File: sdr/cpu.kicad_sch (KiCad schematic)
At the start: 6 parts, among them U4 CH32V305RBT6

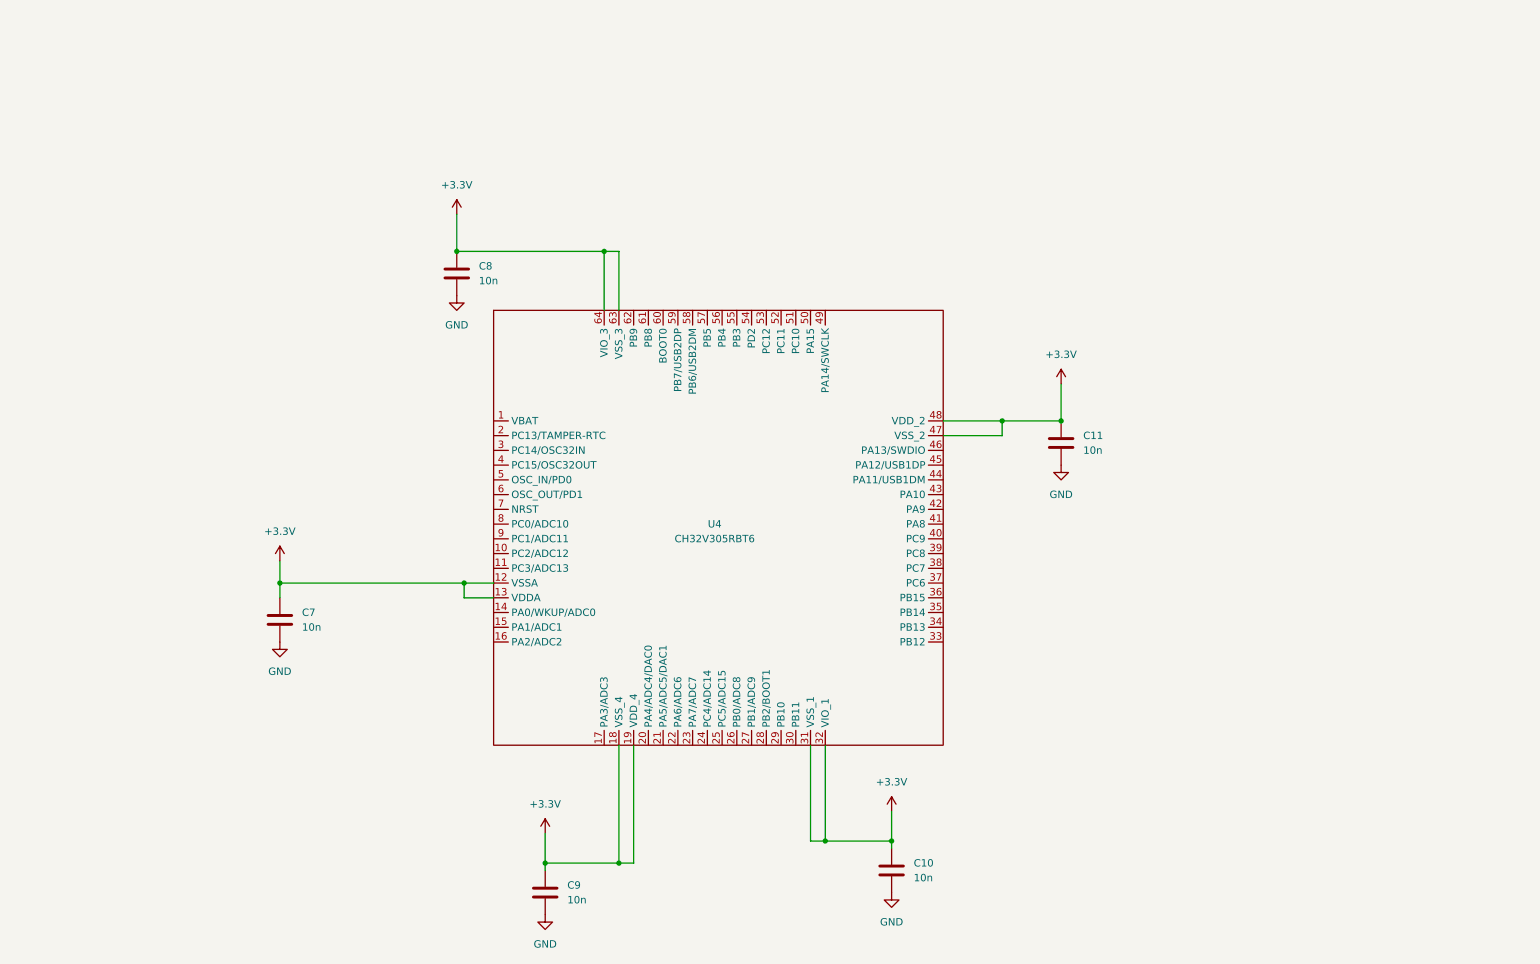
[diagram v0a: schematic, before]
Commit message: Update lots of things. Now have basic CPU as well as some crude mixers
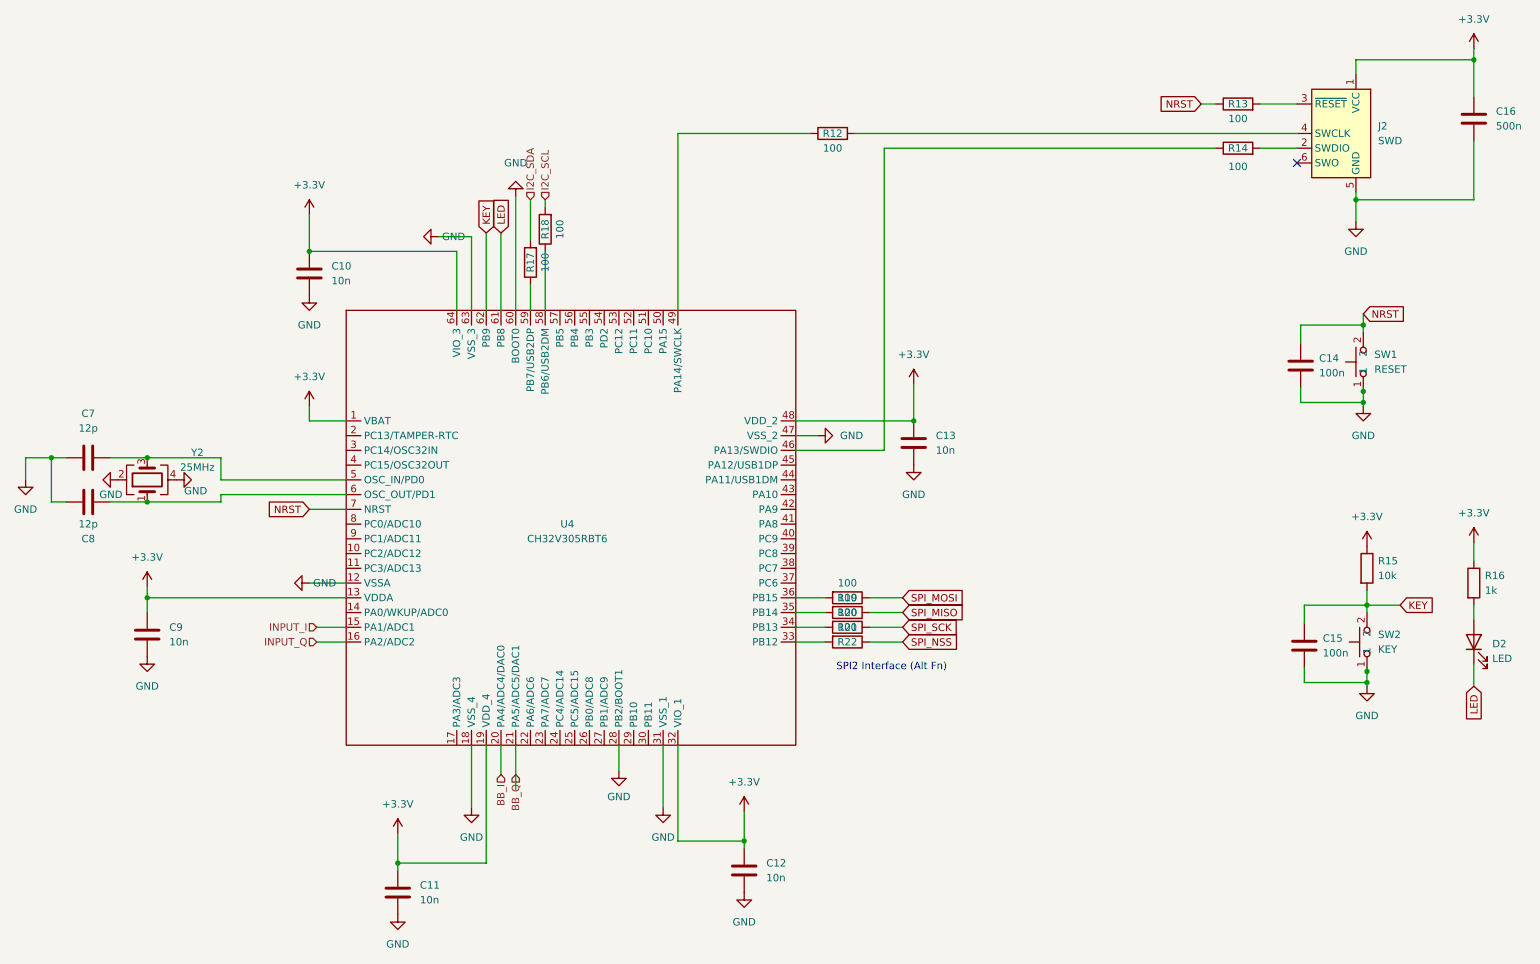
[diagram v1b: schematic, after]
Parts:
- added C14, C15: 100n, Capacitor_SMD:C_0201_0603Metric, symbol Device:C
- added C16: 500n, Capacitor_SMD:C_0201_0603Metric, symbol Device:C
- added C7, C8: 12p, Capacitor_SMD:C_0201_0603Metric, symbol Device:C
- added D2: LED, Diode_SMD:D_0603_1608Metric, symbol Device:LED
- added J2: SWD, Connector:Tag-Connect_TC2030-IDC-NL_2x03_P1.27mm_Vertical, symbol Connector:Conn_ARM_SWD_TagConnect_TC2030-NL
- added R12, R13, R14, R17, R18, R19, R20, R21, R22: 100, Resistor_SMD:R_0402_1005Metric, symbol Device:R
- added R15: 10k, Resistor_SMD:R_0402_1005Metric, symbol Device:R
- added R16: 1k, Resistor_SMD:R_0402_1005Metric, symbol Device:R
- added SW1: RESET, ZL4AA:TS-1187A-B-A-B, symbol zl4aa:TS-1187A-B-A-B
- added SW2: KEY, ZL4AA:TS-1187A-B-A-B, symbol zl4aa:TS-1187A-B-A-B
- added Y2: 25MHz, Crystal:Crystal_SMD_3225-4Pin_3.2x2.5mm, symbol Device:Crystal_GND24
- C10: renamed from C8; footprint (none) -> Capacitor_SMD:C_0201_0603Metric
- C11: renamed from C9; footprint (none) -> Capacitor_SMD:C_0201_0603Metric
- C12: renamed from C10; footprint (none) -> Capacitor_SMD:C_0201_0603Metric
- C13: renamed from C11; footprint (none) -> Capacitor_SMD:C_0201_0603Metric
- C9: renamed from C7; footprint (none) -> Capacitor_SMD:C_0201_0603Metric
- U4: footprint (none) -> Package_QFP:LQFP-64_10x10mm_P0.5mm
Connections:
- net +3.3V: now also U4.1 (VBAT), C16.1, J2.1 (VCC), R15.1, R16.1; no longer U4.12 (VSSA), U4.18 (VSS_4), U4.31 (VSS_1), U4.47 (VSS_2), U4.63 (VSS_3)
- net GND: now also U4.12 (VSSA), U4.18 (VSS_4), U4.28 (PB2/BOOT1), U4.31 (VSS_1), U4.47 (VSS_2), U4.60 (BOOT0), U4.63 (VSS_3), C14.2, C15.2, C16.2, C7.1, C8.1, J2.5 (GND), SW1.1, SW2.1, Y2.2, Y2.4
- net INPUT_I: now reaches U4.15 (PA1/ADC1)
- net INPUT_Q: now reaches U4.16 (PA2/ADC2)
- net BB_I: now reaches U4.20 (PA4/ADC4/DAC0)
- net BB_Q: now reaches U4.21 (PA5/ADC5/DAC1)
- net at U4.33 (PB12): now also R22.2
- net at U4.34 (PB13): now also R21.2
- net at U4.35 (PB14): now also R20.2
- net at U4.36 (PB15): now also R19.2
- net at U4.46 (PA13/SWDIO): now also R14.1
- net at U4.49 (PA14/SWCLK): now also R12.1
- net at U4.5 (OSC_IN/PD0): now also C7.2, Y2.3
- net at U4.58 (PB6/USB2DM): now also R18.1
- net at U4.59 (PB7/USB2DP): now also R17.1
- net at U4.6 (OSC_OUT/PD1): now also C8.2, Y2.1
- net LED: now reaches U4.61 (PB8)
- net LED: now also D2.1 (K)
- net KEY: now reaches U4.62 (PB9)
- net KEY: now also C15.1, R15.2, SW2.2
- net NRST: now reaches U4.7 (NRST)
- net NRST: now also C14.1, R13.1, SW1.2
- new net: J2.2 (SWDIO), R14.2
- new net: J2.3 (~{RESET}), R13.2
- new net: J2.4 (SWCLK), R12.2
- new net: D2.2 (A), R16.2
- new net I2C_SCL: R18.2
- new net I2C_SDA: R17.2
- new net SPI_MISO: R20.1
- new net SPI_MOSI: R19.1
- new net SPI_NSS: R22.1
- new net SPI_SCK: R21.1
- no-connect marks 0 -> 1
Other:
- note added: "SPI2 Interface (Alt Fn)"
- moved on the sheet: C10, C11, C12, C13, C9, U4

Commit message: Added ST-link 6-pin 0.1 programming header
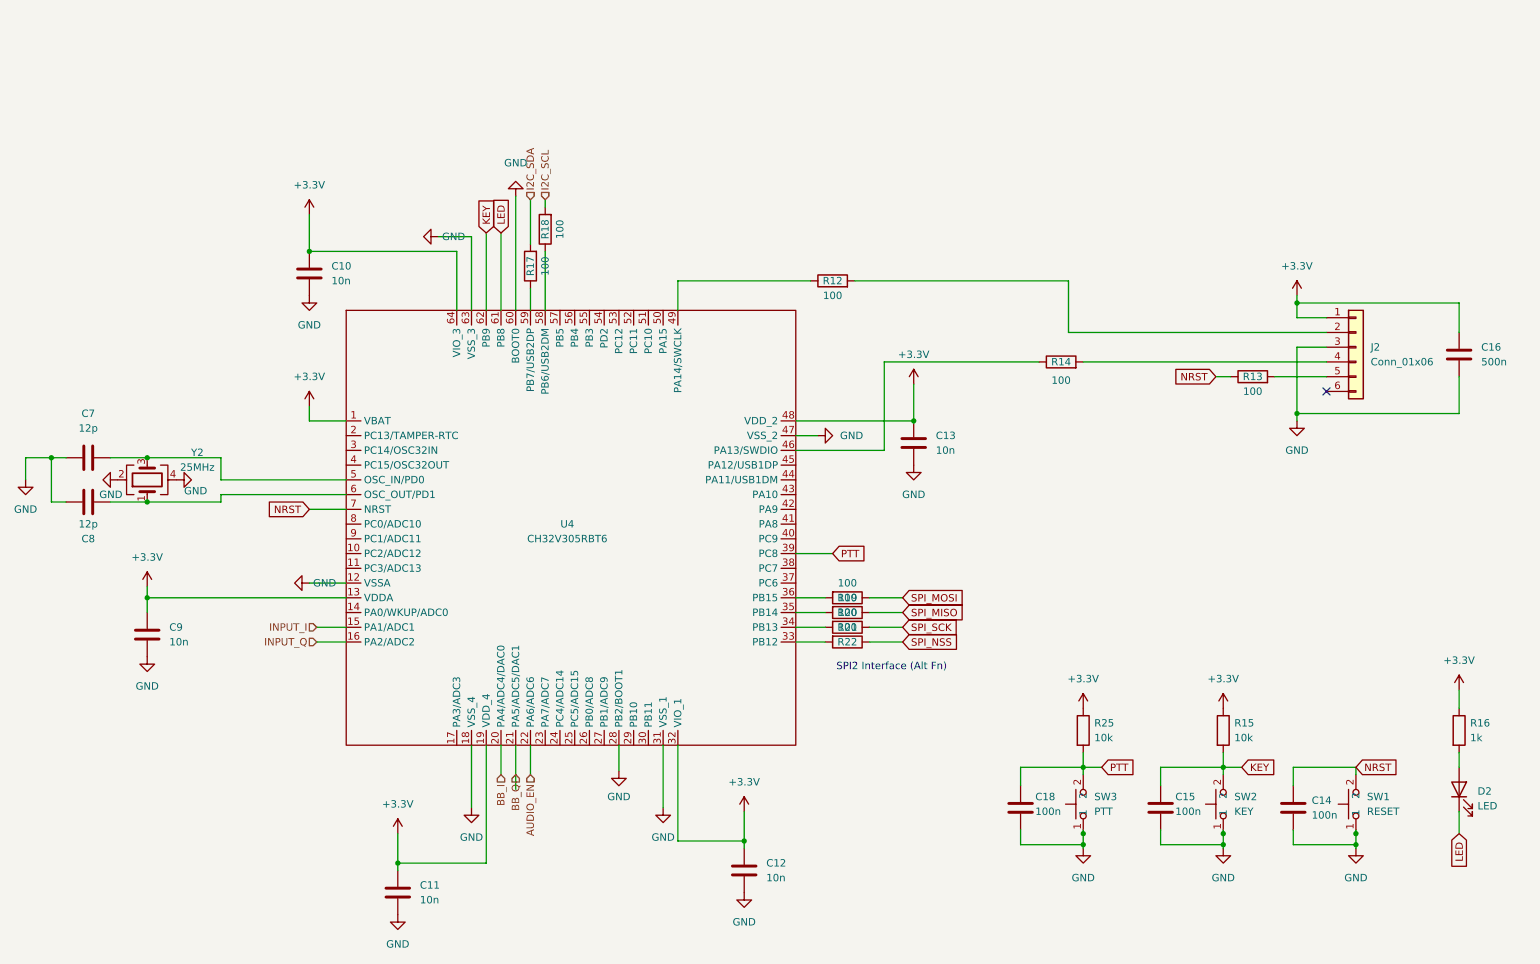
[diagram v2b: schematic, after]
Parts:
- removed J2: SWD, Connector:Tag-Connect_TC2030-IDC-NL_2x03_P1.27mm_Vertical, symbol Connector:Conn_ARM_SWD_TagConnect_TC2030-NL
- added C18: 100n, Capacitor_SMD:C_0603_1608Metric, symbol Device:C
- added J2: Conn_01x06, Connector_PinHeader_2.54mm:PinHeader_1x06_P2.54mm_Horizontal, symbol Connector_Generic:Conn_01x06
- added R25: 10k, Resistor_SMD:R_0402_1005Metric, symbol Device:R
- added SW3: PTT, ZL4AA:TS-1187A-B-A-B, symbol zl4aa:TS-1187A-B-A-B
- C10, C11, C12, C13, C14, C15, C16, C7, C8, C9: footprint Capacitor_SMD:C_0201_0603Metric -> Capacitor_SMD:C_0603_1608Metric
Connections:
- net +3.3V: now also J2.1 (Pin_1), R25.1
- net GND: now also C18.2, J2.3 (Pin_3), SW3.1
- net at R14.2: now also J2.4 (Pin_4)
- net at R13.2: now also J2.5 (Pin_5)
- net at R12.2: now also J2.2 (Pin_2)
- net AUDIO_EN: now reaches U4.22 (PA6/ADC6)
- net PTT: now reaches U4.39 (PC8)
- net PTT: now also C18.1, R25.2, SW3.2
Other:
- moved on the sheet: C14, C15, C16, D2, R12, R13, R14, R15, R16, R17, SW1, SW2

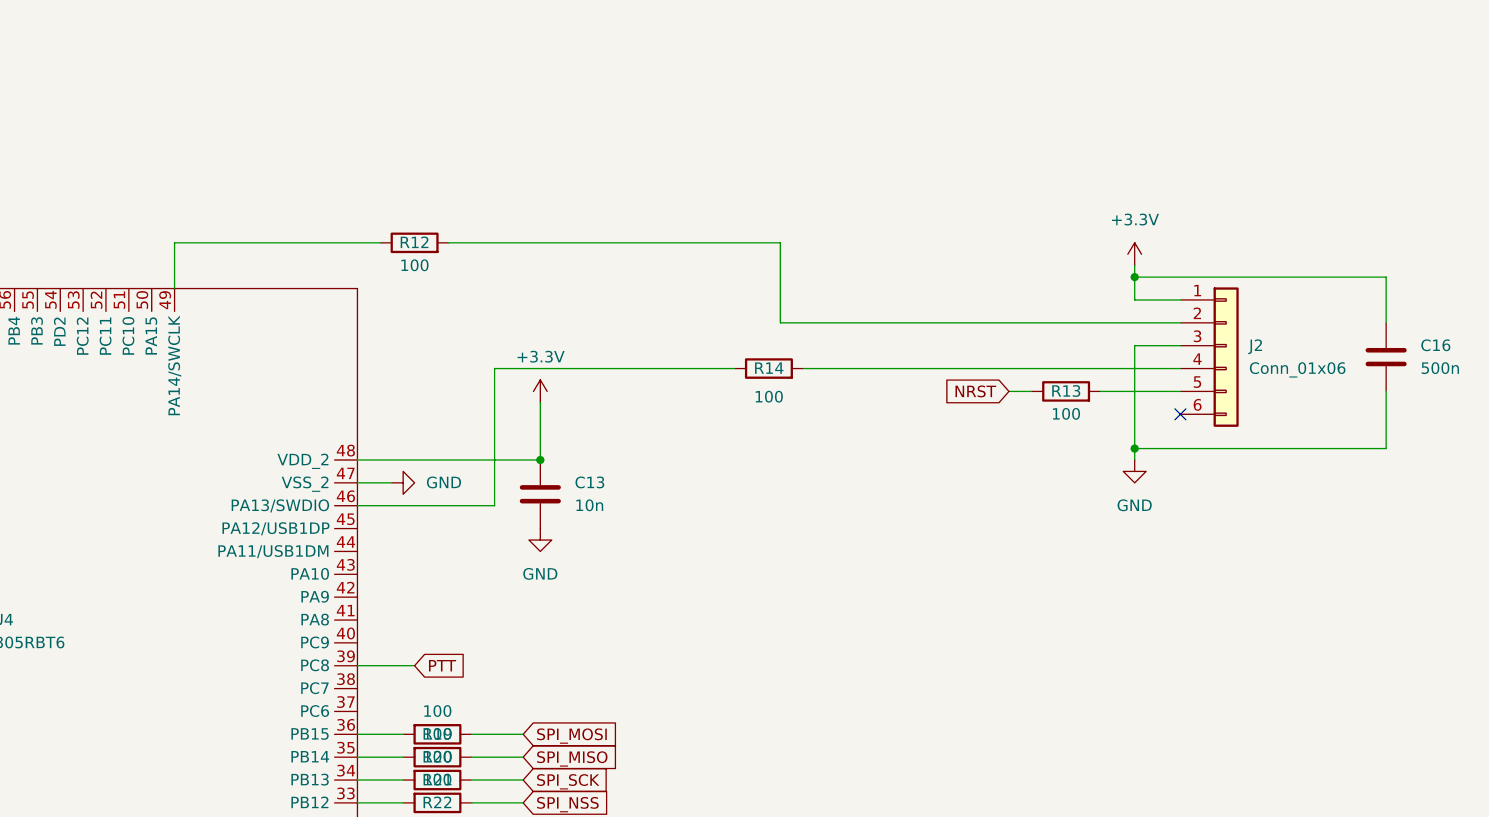
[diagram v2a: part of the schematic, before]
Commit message: Tighten up design layout.
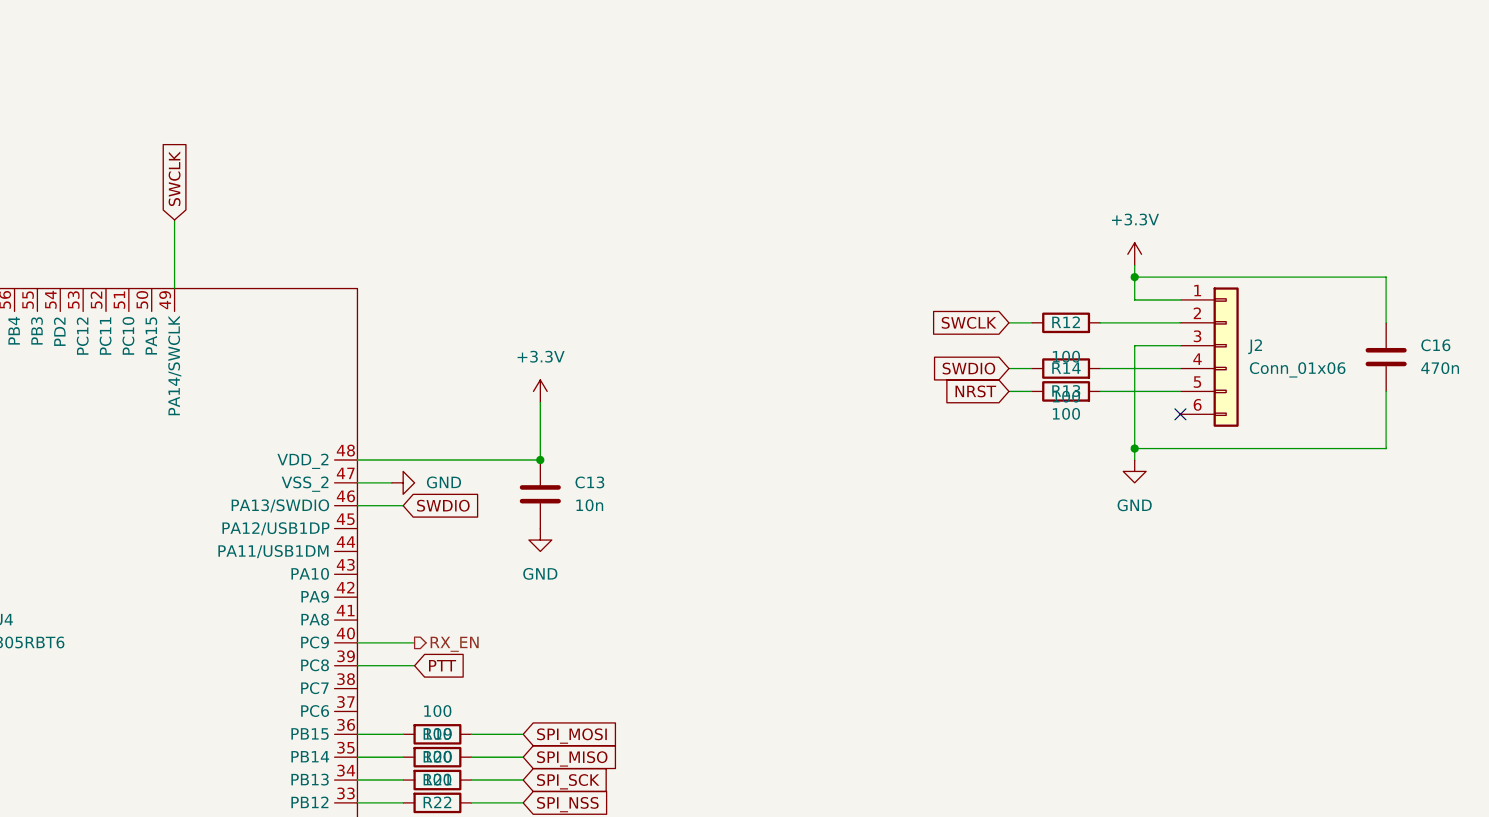
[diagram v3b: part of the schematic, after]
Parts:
- C10, C11, C12, C13, C14, C15, C18, C7, C8, C9: footprint Capacitor_SMD:C_0603_1608Metric -> Capacitor_SMD:C_0402_1005Metric
- C16: value 500n -> 470n
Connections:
- net SWCLK: now reaches R12.1, U4.49 (PA14/SWCLK)
- net RX_EN: now reaches U4.40 (PC9)
- net SWDIO: now reaches R14.1, U4.46 (PA13/SWDIO)
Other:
- moved on the sheet: R12, R14

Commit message: Many fixes. Updated mixers to use the analog switches rather than discretes.
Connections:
- net BB_I renamed DAC_I
- net BB_Q renamed DAC_Q
- net INPUT_I renamed ADC_I
- net INPUT_Q renamed ADC_Q
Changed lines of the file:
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@@
     (stroke (width 0) (type default) (color 0 0 0 0))
   )
-  (wire (pts (xy 102.87 139.7) (xy 102.87 144.78))
+  (wire (pts (xy 102.87 139.7) (xy 102.87 148.844))
     (stroke (width 0) (type default) (color 0 0 0 0))
   )
@@
     (stroke (width 0) (type default) (color 0 0 0 0))
   )
-  (wire (pts (xy 105.41 139.7) (xy 105.41 147.32))
+  (wire (pts (xy 105.41 139.7) (xy 105.41 148.59))
     (stroke (width 0) (type default) (color 0 0 0 0))
   )
@@
     (effects (font (size 1.27 1.27)) (justify left))
   )
-  (hierarchical_label "INPUT_Q" (shape input) (at 71.12 121.92 180)
-    (effects (font (size 1.27 1.27)) (justify right))
-  )
-  (hierarchical_label "BB_I" (shape input) (at 102.87 144.78 270)
+  (hierarchical_label "ADC_Q" (shape input) (at 71.12 121.92 180)
+    (effects (font (size 1.27 1.27)) (justify right))
+  )
+  (hierarchical_label "DAC_I" (shape input) (at 102.87 148.844 270)
     (effects (font (size 1.27 1.27)) (justify right))
   )
@@
     (effects (font (size 1.27 1.27)) (justify left))
   )
-  (hierarchical_label "BB_Q" (shape input) (at 105.41 144.78 270)
-    (effects (font (size 1.27 1.27)) (justify right))
-  )
-  (hierarchical_label "INPUT_I" (shape input) (at 71.12 119.38 180)
-    (effects (font (size 1.27 1.27)) (justify right))
-  )
+  (hierarchical_label "DAC_Q" (shape input) (at 105.41 148.59 270)
+    (effects (font (size 1.27 1.27)) (justify right))
+  )
+  (hierarchical_label "ADC_I" (shape input) (at 71.12 119.38 180)
+    (effects (font (size 1.27 1.27)) (justify right))
+  )
